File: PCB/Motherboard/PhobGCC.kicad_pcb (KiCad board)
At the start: 2 copper layers, 125.5 x 72.9 mm, 58 parts, among them J1 Conn_01x06_Female, J2 Conn_01x04_Female, J3 Conn_01x01_Male, J5 Conn_01x02_Male, Q1 SSM3K56FS,LF, SW1 A, SW10 Dup, SW11 Dright, SW12 Ddown, SW2 B, SW3 X, SW4 Y, SW5 Start, SW6 L, SW7 R, SW8 1825027-5, SW9 Dleft, U1 Teensy4.0, U2 2x DRV5053CAQLPGM Hall Effect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, U3 BPR-105, U4 BPR-105

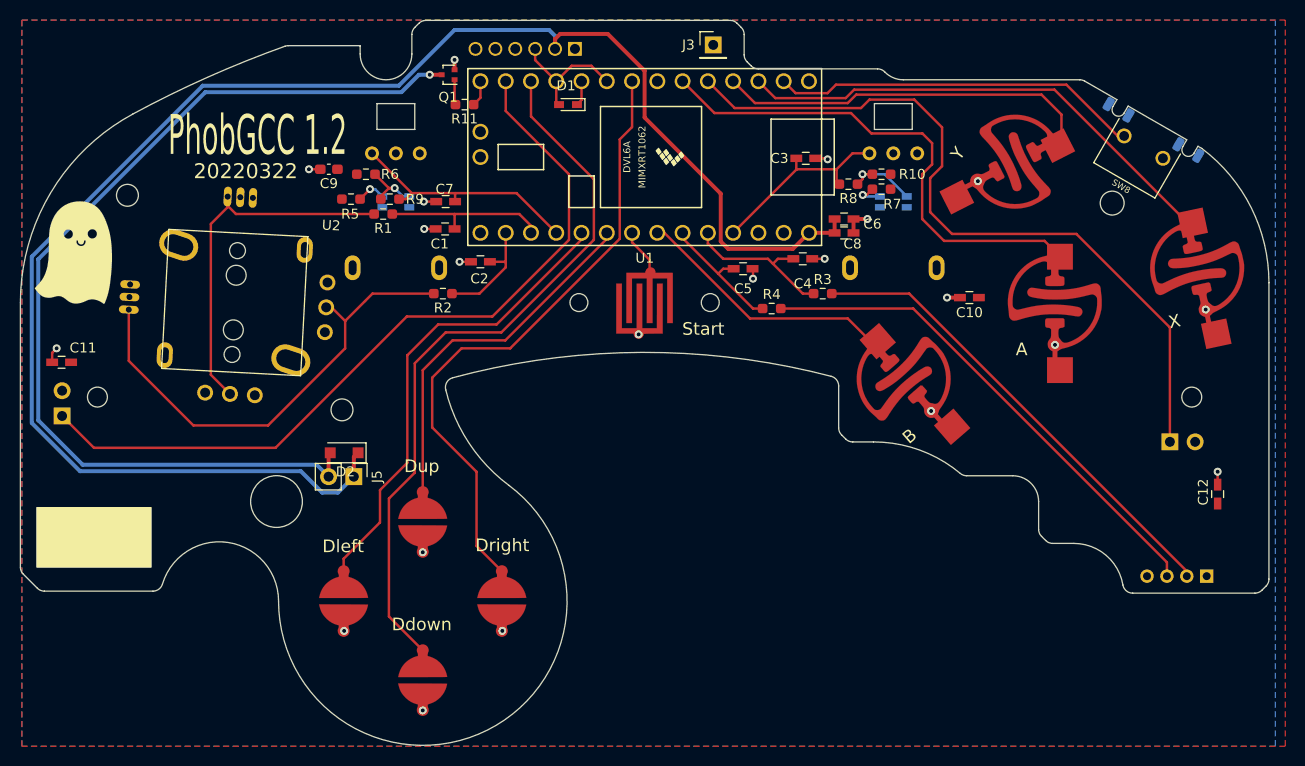
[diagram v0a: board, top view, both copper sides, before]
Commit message: Tidied up some things in the PCB, redid the ABXY contacts from an earlier file version, preview now works on jlcPCB
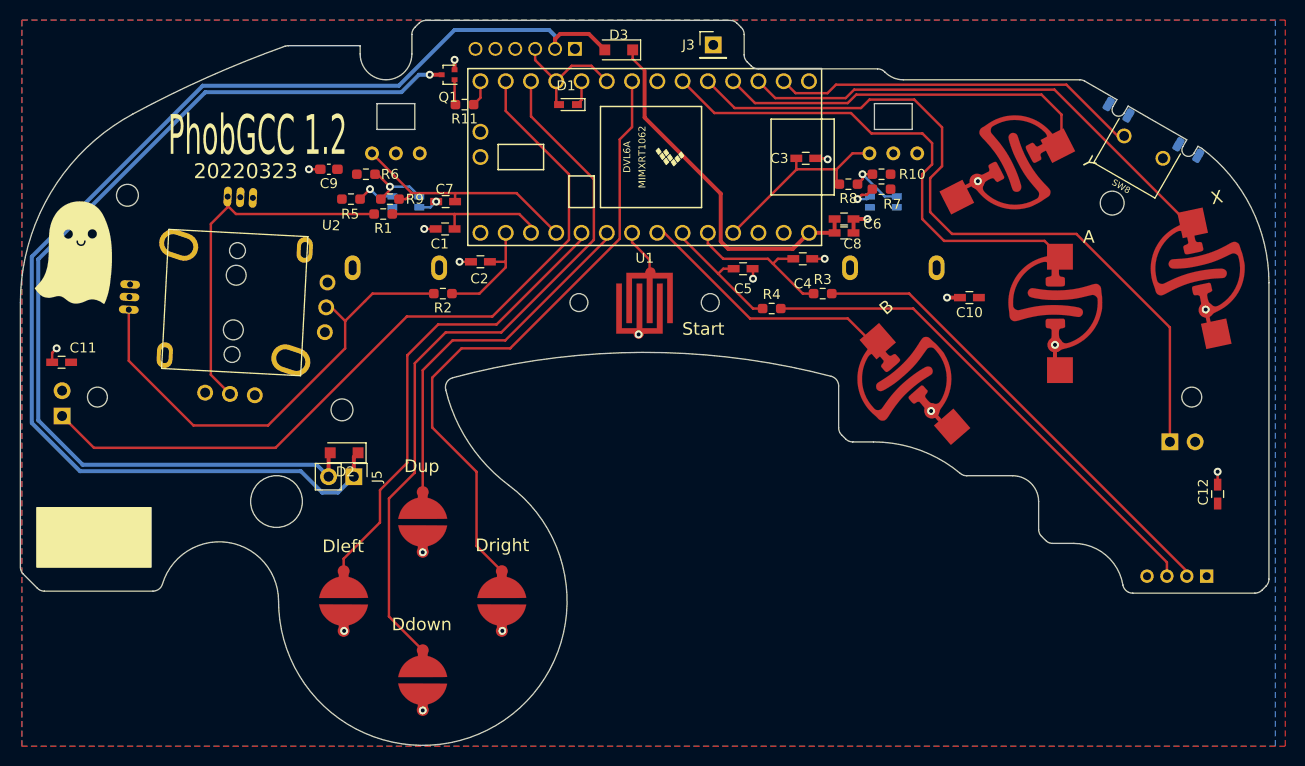
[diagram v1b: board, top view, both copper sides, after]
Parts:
- added D3: M7C, Diode_SMD:D_SOD-123F, F.Cu at (110.0, 53.0)
- SW1, SW2, SW3, SW4: footprint Gamecube MB:ABXY_layout_small_mask_omron_switch2 -> Gamecube MB:ABXY_Contact_Omron_Switch
- moved U3 1.00 mm to (88.6, 68.3)
- moved U4 1.00 mm to (136.6, 68.3)
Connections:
- C6 pad 1: +5V -> Net-(U1-Pad33)
- C8 pad 1: +5V -> Net-(U1-Pad33)
- U1 pad 33: +5V -> Net-(U1-Pad33)
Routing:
- net +5V: track 165.7 -> 126.7 mm
- net Net-(U1-Pad33): track 0.00 -> 36.7 mm
- net Net-(R10-Pad2): track 7.58 -> 6.58 mm
- net Net-(R5-Pad2): track 2.96 -> 3.96 mm
- net Net-(R6-Pad2): track 6.39 -> 7.29 mm
- net GND: track 16.5 -> 17.2 mm
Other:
- board text added: "20220323"
- board text removed: "20220322"

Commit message: Cleaned up the silkscreen a little bit
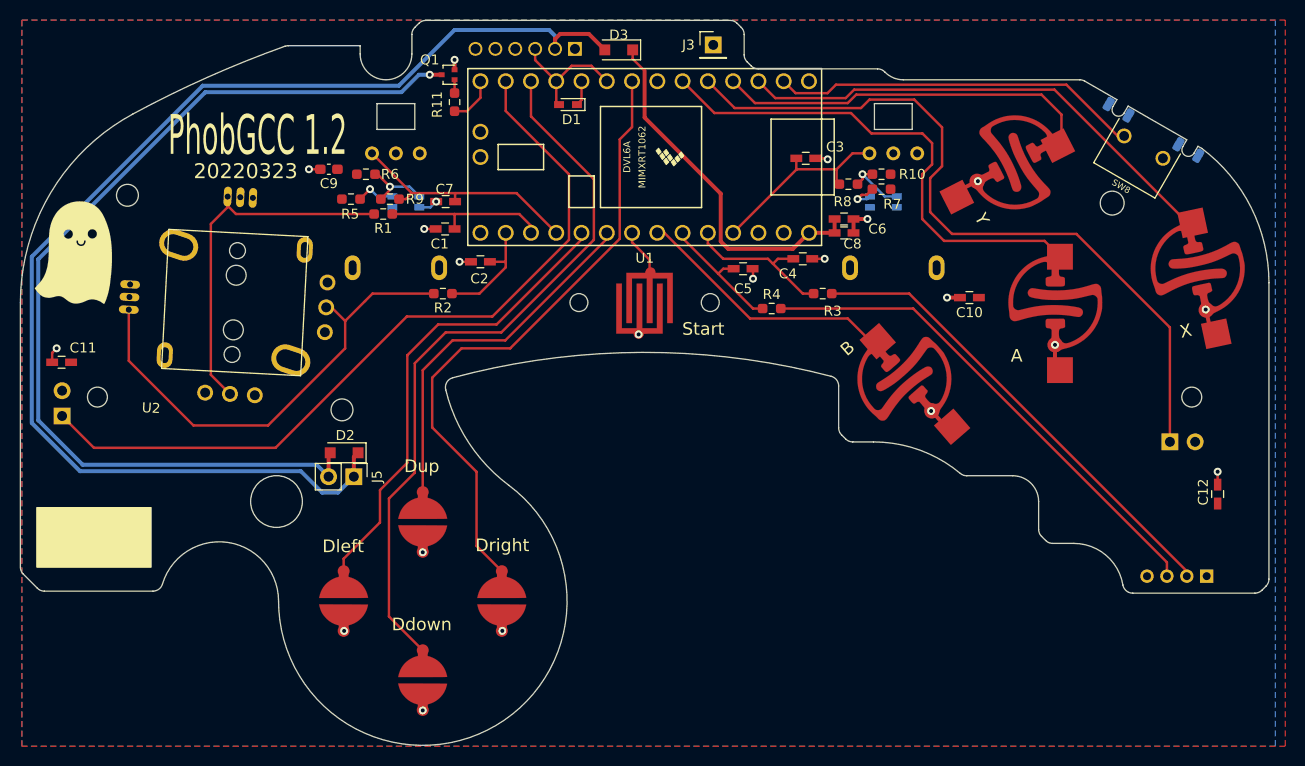
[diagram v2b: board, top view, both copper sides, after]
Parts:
- moved R11 1.03 mm to (93.5, 58.2), turned to 90 degrees
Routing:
- net /Rumble: track 2.63 -> 4.82 mm
- net Net-(Q1-Pad1): track 2.54 -> 1.34 mm
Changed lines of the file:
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@@
       (effects (font (size 1.27 1.27) (thickness 0.15)))
     )
-    (fp_text value "A" (at 3.4 -6.55) (layer "F.SilkS")
+    (fp_text value "A" (at -3.85 5.4) (layer "F.SilkS")
       (effects (font (size 1.27 1.27) (thickness 0.15)))
     )
@@
       (effects (font (size 1.27 1.27) (thickness 0.15)))
     )
-    (fp_text value "B" (at 3.4 -6.55 41) (layer "F.SilkS")
+    (fp_text value "B" (at -2.263129 -6.008598 41) (layer "F.SilkS")
       (effects (font (size 1.27 1.27) (thickness 0.15)))
     )
@@
     (property "Sheetname" "")
     (attr through_hole)
-    (fp_text reference "U2" (at 9.275 -8.25 177) (layer "F.SilkS")
+    (fp_text reference "U2" (at -7.83871 11.027127 -3 unlocked) (layer "F.SilkS")
       (effects (font (size 1 1) (thickness 0.15)))
     )
@@
     (property "Sheetname" "")
     (attr smd)
-    (fp_text reference "C3" (at -2.65 0) (layer "F.SilkS")
+    (fp_text reference "C3" (at 2.95 -1.15) (layer "F.SilkS")
       (effects (font (size 1 1) (thickness 0.15)))
     )
@@
     (property "Sheetname" "")
     (attr smd)
-    (fp_text reference "C4" (at 0 2.5) (layer "F.SilkS")
+    (fp_text reference "C4" (at -1.5 1.5) (layer "F.SilkS")
       (effects (font (size 1 1) (thickness 0.15)))
     )
@@
       (effects (font (size 1.27 1.27) (thickness 0.15)))
     )
-    (fp_text value "Y" (at 3.4 -6.55 -63) (layer "F.SilkS")
+    (fp_text value "Y" (at 3.602419 5.595317 -63 unlocked) (layer "F.SilkS")
       (effects (font (size 1.27 1.27) (thickness 0.15)))
     )
@@
       (effects (font (size 1.27 1.27) (thickness 0.15)))
     )
-    (fp_text value "X" (at 3.4 -6.55 12) (layer "F.SilkS")
+    (fp_text value "X" (at -2.434713 5.923231 12) (layer "F.SilkS")
       (effects (font (size 1.27 1.27) (thickness 0.15)))
     )
@@
     (property "Sheetname" "")
     (attr smd)
-    (fp_text reference "D1" (at 0.2 1.9) (layer "F.SilkS")
+    (fp_text reference "D1" (at -0.35 -1.5) (layer "F.SilkS")
       (effects (font (size 1 1) (thickness 0.15)))
     )
@@
     (property "Sheetname" "")
     (attr smd)
-    (fp_text reference "C6" (at 2.85 0.5) (layer "F.SilkS")
+    (fp_text reference "C6" (at 3.35 1) (layer "F.SilkS")
       (effects (font (size 1 1) (thickness 0.15)))
     )
@@
     (property "Sheetname" "")
     (attr smd)
-    (fp_text reference "R3" (at 0 -1.43) (layer "F.SilkS")
+    (fp_text reference "R3" (at 1 1.75) (layer "F.SilkS")
       (effects (font (size 1 1) (thickness 0.15)))
     )
@@
     (property "Sheetname" "")
     (attr smd)
-    (fp_text reference "R8" (at 0 -1.43) (layer "F.SilkS")
+    (fp_text reference "R8" (at 0.5875 -1.75) (layer "F.SilkS")
       (effects (font (size 1 1) (thickness 0.15)))
     )
@@
     (property "Sheetname" "")
     (attr smd)
-    (fp_text reference "Q1" (at 0 -2.25) (layer "F.SilkS")
+    (fp_text reference "Q1" (at 1.85 1.5) (layer "F.SilkS")
       (effects (font (size 1 1) (thickness 0.15)))
     )
@@
     (property "Sheetname" "")
     (attr smd)
-    (fp_text reference "D2" (at -0.127 -1.905) (layer "F.SilkS")
+    (fp_text reference "D2" (at -0.1 1.75) (layer "F.SilkS")
       (effects (font (size 1 1) (thickness 0.15)))
     )
@@
   )
   (footprint "Resistor_SMD:R_0603_1608Metric_Pad0.98x0.95mm_HandSolder" (layer "F.Cu")
-    (at 94.5 58.5 180)
+    (at 93.5 58.25 90)
     (descr "Resistor SMD 0603 (1608 Metric), square (rectangular) end terminal, IPC_7351 nominal with elongated pad for handsoldering. (Body size source: IPC-SM-782 page 72, https://www.pcb-3d.com/wordpress/wp-content/uploads/ipc-sm-782a_amendment_1_and_2.pdf), generated with kicad-footprint-generator")
     (tags "resistor handsolder")
@@
     (property "Sheetname" "")
     (attr smd)
-    (fp_text reference "R11" (at 0 -1.43) (layer "F.SilkS")
+    (fp_text reference "R11" (at -0.25 -1.75 90) (layer "F.SilkS")
       (effects (font (size 1 1) (thickness 0.15)))
     )
-    (fp_text value "330R" (at 0 1.43) (layer "F.Fab")
+    (fp_text value "330R" (at 0 1.43 90) (layer "F.Fab")
       (effects (font (size 1 1) (thickness 0.15)))
     )
-    (fp_text user "${REFERENCE}" (at 0 0) (layer "F.Fab")
+    (fp_text user "${REFERENCE}" (at 0 0 90) (layer "F.Fab")
       (effects (font (size 0.4 0.4) (thickness 0.06)))
     )
@@
     (fp_line (start 0.8 0.4125) (end -0.8 0.4125) (layer "F.Fab") (width 0.1))
     (fp_line (start -0.8 -0.4125) (end 0.8 -0.4125) (layer "F.Fab") (width 0.1))
-    (pad "1" smd roundrect (at -0.9125 0 180) (size 0.975 0.95) (layers "F.Cu" "F.Paste" "F.Mask") (roundrect_rratio 0.25)
+    (pad "1" smd roundrect (at -0.9125 0 90) (size 0.975 0.95) (layers "F.Cu" "F.Paste" "F.Mask") (roundrect_rratio 0.25)
       (net 29 "/Rumble") (pintype "passive"))
-    (pad "2" smd roundrect (at 0.9125 0 180) (size 0.975 0.95) (layers "F.Cu" "F.Paste" "F.Mask") (roundrect_rratio 0.25)
+    (pad "2" smd roundrect (at 0.9125 0 90) (size 0.975 0.95) (layers "F.Cu" "F.Paste" "F.Mask") (roundrect_rratio 0.25)
       (net 37 "Net-(Q1-Pad1)") (pintype "passive"))
     (model "${KICAD6_3DMODEL_DIR}/Resistor_SMD.3dshapes/R_0603_1608Metric.wrl"
@@
   (segment (start 88.169039 57.24952) (end 89.91856 55.5) (width 0.4) (layer "B.Cu") (net 27))
   (segment (start 80.835 95.9) (end 79.63596 94.70096) (width 0.4) (layer "B.Cu") (net 27))
-  (segment (start 96.1 57.8125) (end 95.4125 58.5) (width 0.25) (layer "F.Cu") (net 29))
-  (segment (start 96.1 56.15) (end 96.1 57.8125) (width 0.25) (layer "F.Cu") (net 29))
+  (segment (start 94.75 59.1625) (end 96.1 57.8125) (width 0.25) (layer "F.Cu") (net 29))
+  (segment (start 96.1 57.8125) (end 96.1 56.15) (width 0.25) (layer "F.Cu") (net 29))
+  (segment (start 93.5 59.1625) (end 94.75 59.1625) (width 0.25) (layer "F.Cu") (net 29))
   (segment (start 126 74) (end 125.5 74.5) (width 0.25) (layer "F.Cu") (net 31))
   (segment (start 120.5 74) (end 125 74) (width 0.25) (layer "F.Cu") (net 31))
@@
   (segment (start 131.69 71.39) (end 131.7 71.4) (width 0.4) (layer "F.Cu") (net 36))
   (segment (start 111.4 53) (end 111.4 53.9) (width 0.25) (layer "F.Cu") (net 36))
-  (segment (start 93.5 58.4125) (end 93.5875 58.5) (width 0.25) (layer "F.Cu") (net 37))
-  (segment (start 93.5 56) (end 93.5 58.4125) (width 0.25) (layer "F.Cu") (net 37))
+  (segment (start 93.5 57.3375) (end 93.5 56) (width 0.25) (layer "F.Cu") (net 37))
   (segment (start 134.5 65.5) (end 135.5 65.5) (width 0.25) (layer "F.Cu") (net 38))
   (segment (start 134.5 66) (end 134 66.5) (width 0.25) (layer "F.Cu") (net 38))

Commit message: More cleanup and teaking of the PCBs, made BOM and placement files for JLC
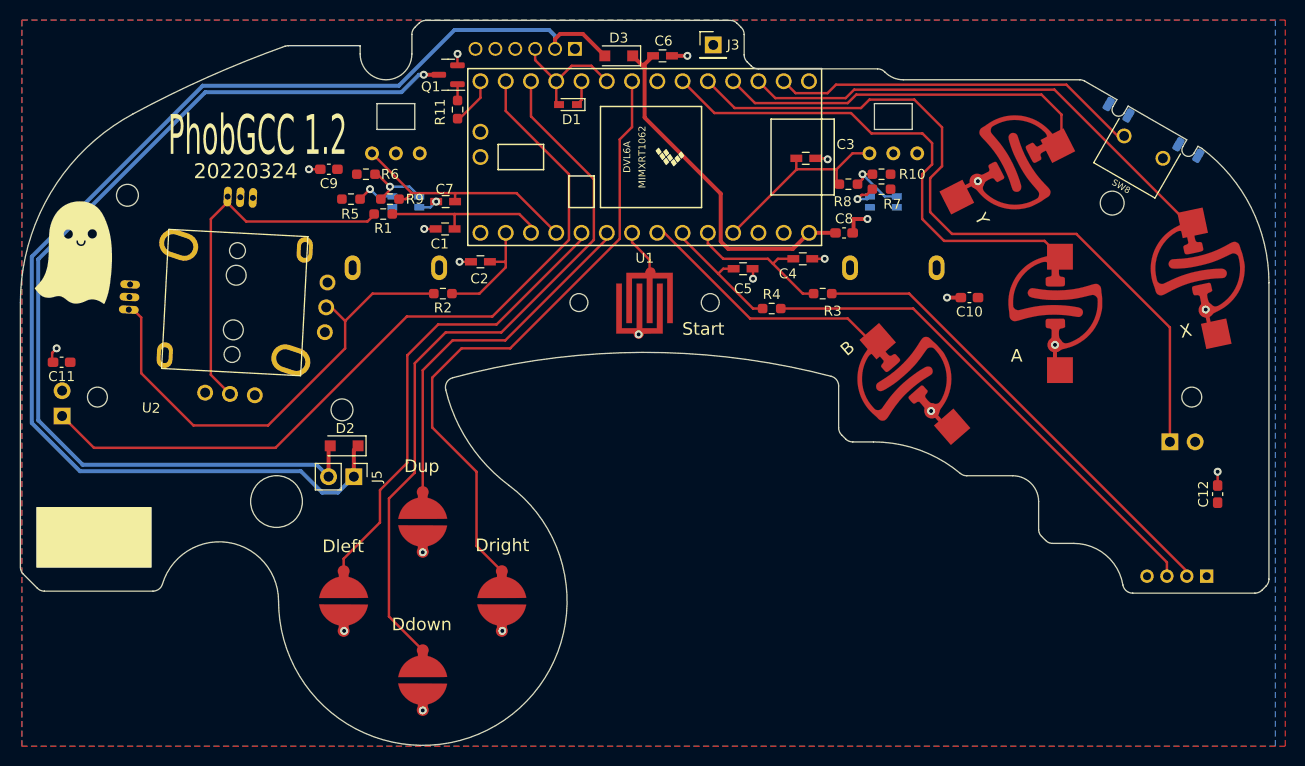
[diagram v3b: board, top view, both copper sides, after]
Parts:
- C10, C11, C12, C8: footprint Capacitors_SMD:C_0603_HandSoldering -> Capacitor_SMD:C_0603_1608Metric_Pad1.08x0.95mm_HandSolder
- Q1: footprint Package_TO_SOT_SMD:SOT-416 -> Package_TO_SOT_SMD:SOT-23
- U3, U4: value BPR-105 -> GP2S60-MFG
- moved C6 24.5 mm to (114.4, 53.6)
- moved R11 0.81 mm to (93.8, 59.0)
- moved D2 0.70 mm to (82.4, 92.8)
- moved D3 0.60 mm to (110.0, 53.6)
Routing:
- net GND: track 17.2 -> 18.6 mm, vias 21 -> 22
- net Net-(D2-Pad2): track 98.4 -> 99.1 mm
- net /X: track 50.8 -> 50.2 mm
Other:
- board text added: "20220324"
- board text removed: "20220323"
